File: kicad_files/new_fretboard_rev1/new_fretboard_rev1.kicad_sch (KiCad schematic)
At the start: 22 parts, among them U2 LX3302AQPW-TR-EASY

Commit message: stm32 micro added
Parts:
- added C100: 4.7uf, Capacitor_SMD:C_1206_3216Metric, symbol Device:C_US
- added C101, C102, C103, C104, C105, C106, C108: 100nf, Capacitor_SMD:C_0402_1005Metric, symbol Device:C
- added C107: 1uf, Capacitor_SMD:C_1206_3216Metric, symbol Device:C_US
- added C109, C110: 2.2uf, Capacitor_SMD:C_1206_3216Metric, symbol Device:C_US
- added U10: STM32F730V8Tx, Package_QFP:LQFP-100_14x14mm_P0.5mm, symbol MCU_ST_STM32F7:STM32F730V8Tx
- C12, C13, C14, C15, C16, C17, C18, C19, C20, C21, C22, L5, L6, L7, L8, R10, R12, R13, R8, R9, U2: Component Class ch1 -> (none)
- R11: value 10R -> 10k; Component Class ch1 -> (none)
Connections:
- net GND: now also C100.2, C101.2, C102.2, C103.2, C104.2, C105.2, C106.2, C107.2, C108.2, C109.2, C110.2, U10.10 (VSS), U10.19 (VSSA), U10.26 (VSS), U10.49 (VSS), U10.74 (VSS), U10.99 (VSS)
- net sent9: now reaches C18.2, R12.2
- net sent9: now also U10.77 (PA15)
- new net: C109.1, U10.48 (VCAP_1)
- new net: C110.1, U10.73 (VCAP_2)
- new net +3V3: C100.1, C101.1, C102.1, C103.1, C104.1, C105.1, C106.1, C107.1, C108.1, U10.100 (VDD), U10.11 (VDD), U10.20 (VREF+), U10.21 (VDDA), U10.27 (VDD), U10.50 (VDD), U10.6 (VBAT), U10.75 (VDD)
- new net sent1: U10.39 (PE9)
- new net sent2: U10.41 (PE11)
- new net sent3: U10.43 (PE13)
- new net sent4: U10.44 (PE14)
- new net sent5: U10.59 (PD12)
- new net sent6: U10.60 (PD13)
- new net sent7: U10.64 (PC7)
- new net sent8: U10.66 (PC9)
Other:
- added sheet testchannel8 (testchannel8.kicad_sch)
- sheet testchannel1: file testchannel2.kicad_sch -> testchannel1.kicad_sch
- note added: "needs oscillator for stm32, and programming header, maybe boot pin connections? Also needs 7 more programming headers for the lx3302a ics"

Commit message: mcu configured, still needs power connections and spi i2c connections
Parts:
- added C111: 100nf, Capacitor_SMD:C_0402_1005Metric, symbol Device:C
- added J3: FTSH-107-01-L-DV-K-A, Snapeda:SAMTEC_FTSH-107-01-L-DV-K-A, symbol Snapeda:FTSH-107-01-L-DV-K-A
- added R57, R58: 10k, Resistor_SMD:R_0402_1005Metric, symbol Device:R
- added R59, R60, R62, R65, R68, R69, R70, R71, R72, R78, R80, R82, R84, R86, R88, R90, R92, R94: 1k, Resistor_SMD:R_0402_1005Metric, symbol Device:R
- added R61, R63, R64, R66, R67, R73, R74, R75, R76, R77, R79, R81, R83, R85, R87, R89, R91, R93: 2k, Resistor_SMD:R_0402_1005Metric, symbol Device:R
- added R95: 33R, Resistor_SMD:R_0402_1005Metric, symbol Device:R
- added Y1: ASE-25.000MHZ-LC-T, Snapeda:XTAL_ASE-25.000MHZ-LC-T, symbol Snapeda:ASE-25.000MHZ-LC-T
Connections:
- net +3V3: now also C111.1, J3.03, Y1.4 (VDD)
- net GND: now also C111.2, J3.05, J3.07, R58.2, R61.2, R63.2, R64.2, R66.2, R67.2, R73.1, R74.1, R75.1, R76.1, R77.2, R79.2, R81.2, R83.2, R85.2, R87.2, R89.2, R91.2, R93.2, Y1.2 (GND/CASE)
- net sent1: now also R69.1; no longer U10.39 (PE9)
- net sent2: now also R70.1; no longer U10.41 (PE11)
- net sent3: now also R71.1; no longer U10.43 (PE13)
- net sent4: now also R72.1; no longer U10.44 (PE14)
- net sent5: now also R65.2; no longer U10.59 (PD12)
- net sent6: now also R67.1, R68.1; no longer U10.60 (PD13)
- net sent7: now also R60.1; no longer U10.64 (PC7)
- net sent8: now also R62.1; no longer U10.66 (PC9)
- net sent9: now also R59.1; no longer U10.77 (PA15)
- net at U10.12 (PH0): now also R57.1
- net nrst: now reaches U10.14 (NRST)
- net nrst: now also J3.12
- net SPI1_NSS: now reaches U10.28 (PA4)
- net SPI1_SCK: now reaches U10.29 (PA5)
- net at U10.30 (PA6): now also R95.2
- net SPI1_MOSI: now reaches U10.31 (PA7)
- net PWM5in: now reaches U10.34 (PB0)
- net PWM5in: now also R85.1, R86.2
- net PWM6in: now reaches U10.35 (PB1)
- net PWM6in: now also R87.1, R88.2
- net PWM8in: now reaches U10.46 (PB10)
- net PWM8in: now also R91.1, R92.2
- net PWM9in: now reaches U10.47 (PB11)
- net PWM9in: now also R93.1, R94.2
- net PWM1in: now reaches U10.61 (PD14)
- net PWM1in: now also R77.1, R78.2
- net PWM2in: now reaches U10.62 (PD15)
- net PWM2in: now also R79.1, R80.2
- net PWM3in: now reaches U10.63 (PC6)
- net PWM3in: now also R81.1, R82.2
- net PWM4in: now reaches U10.65 (PC8)
- net PWM4in: now also R83.1, R84.2
- net swdio: now reaches U10.72 (PA13)
- net swdio: now also J3.04
- net swclk: now reaches U10.76 (PA14)
- net swclk: now also J3.06
- net swo: now reaches U10.89 (PB3)
- net swo: now also J3.08
- net PWM7in: now reaches U10.90 (PB4)
- net PWM7in: now also R89.1, R90.2
- net I2C_SCL: now reaches U10.92 (PB6)
- net I2C_SDA: now reaches U10.93 (PB7)
- net at U10.94 (BOOT0): now also R58.1
- net PWM9send: now reaches U2.7 (IO1)
- net PWM9send: now also R94.1
- net GLOBAL_VIN: now reaches C20.2, R13.2
- new net: R62.2, R63.1, U10.66 (PC9)
- new net: R70.2, R74.2, U10.41 (PE11)
- new net: R69.2, R73.2, U10.39 (PE9)
- new net: R57.2, Y1.3 (OUTPUT)
- new net: R59.2, R64.1, U10.77 (PA15)
- new net: R71.2, R75.2, U10.43 (PE13)
- new net: R72.2, R76.2, U10.44 (PE14)
- new net: R65.1, R66.1, U10.59 (PD12)
- new net: R68.2, U10.60 (PD13)
- new net: R60.2, R61.1, U10.64 (PC7)
- new net PWM1send: R78.1
- new net PWM2send: R80.1
- new net PWM3send: R82.1
- new net PWM4send: R84.1
- new net PWM5send: R86.1
- new net PWM6send: R88.1
- new net PWM7send: R90.1
- new net PWM8send: R92.1
- new net SPI1_MISO: R95.1
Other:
- note removed: "needs oscillator for stm32, and programming header, maybe boot pin connections? Also needs 7 more programming headers for the lx3302a ics"

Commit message: finished routing - adding silkscreen
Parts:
- added C112, C113: 1uf, Capacitor_SMD:C_1206_3216Metric, symbol Device:C_US
- added J10: 530470410, Snapeda:CONN04_530470410_MOL, symbol Snapeda:530470410
- added J11, J12, J13: 110990030, Snapeda:SEEED_110990030, symbol Snapeda:110990030
- added R103: 10k, Resistor_SMD:R_0402_1005Metric, symbol Device:R
- added R96: 0R, Resistor_SMD:R_1206_3216Metric, symbol Device:R
- added TP1, TP2, TP3, TP4: TestPoint, Connector_PinHeader_1.00mm:PinHeader_1x01_P1.00mm_Vertical, symbol Connector:TestPoint
- added U11: MIC5504-3.3YM5, Package_TO_SOT_SMD:SOT-23-5, symbol Regulator_Linear:MIC5504-3.3YM5
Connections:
- net +3V3: now also C112.1, U11.5 (VOUT)
- net GLOBAL_VIN: now also J13.1, J13.2, R96.2
- net GND: now also C112.2, C113.2, J10.1, J11.4, J13.3, J13.4, U11.2 (GND)
- net I2C_SCL: now also J11.1
- net I2C_SDA: now also J11.2
- net PWM1in: now also U10.34 (PB0); no longer U10.61 (PD14)
- net PWM2in: now also U10.35 (PB1); no longer U10.62 (PD15)
- net PWM3in: now also U10.46 (PB10); no longer U10.63 (PC6)
- net PWM4in: now also U10.47 (PB11); no longer U10.65 (PC8)
- net PWM5in: now also U10.61 (PD14); no longer U10.34 (PB0)
- net PWM6in: now also U10.62 (PD15); no longer U10.35 (PB1)
- net PWM7in: now also TP2.1; no longer U10.90 (PB4)
- net PWM8in: now also TP1.1; no longer U10.46 (PB10)
- net PWM9in: now also U10.90 (PB4); no longer U10.47 (PB11)
- net SPI1_MISO: now also J12.3
- net SPI1_MOSI: now also J12.4
- net SPI1_NSS: now also J12.2
- net SPI1_SCK: now also J12.1
- net VIN_A: now also J10.2, R103.2
- net IO3: now reaches U2.3 (IO3)
- net IO3: now also J10.3, R103.1
- net IO2: now reaches C19.2, R11.1, R12.1, U2.6 (IO2)
- net IO2: now also J10.4
- new net: TP3.1, U10.63 (PC6)
- new net: TP4.1, U10.65 (PC8)
- new net GLOBAL_VIN2: C113.1, R96.1, U11.1 (VIN), U11.3 (EN)

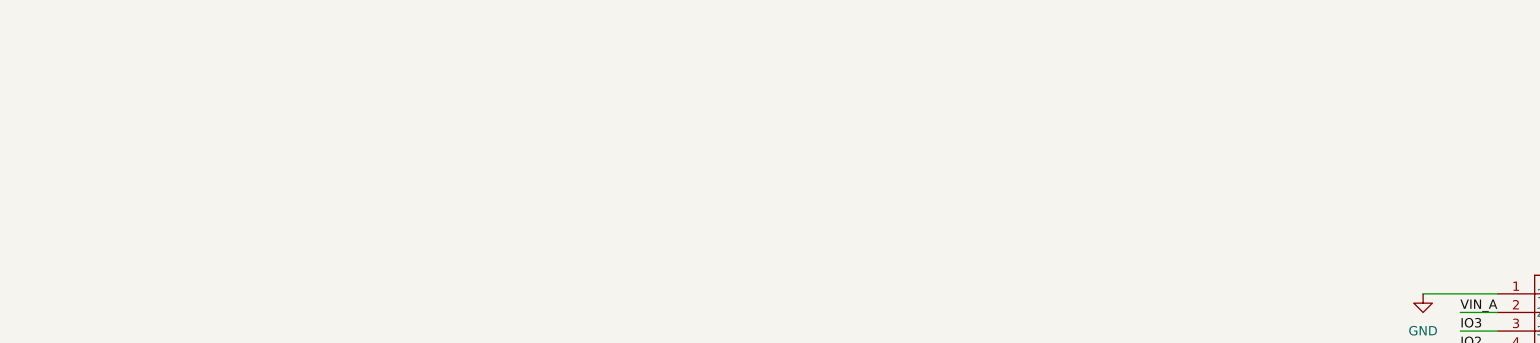
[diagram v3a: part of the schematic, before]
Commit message: mostly done, adjusting silkscreen labels
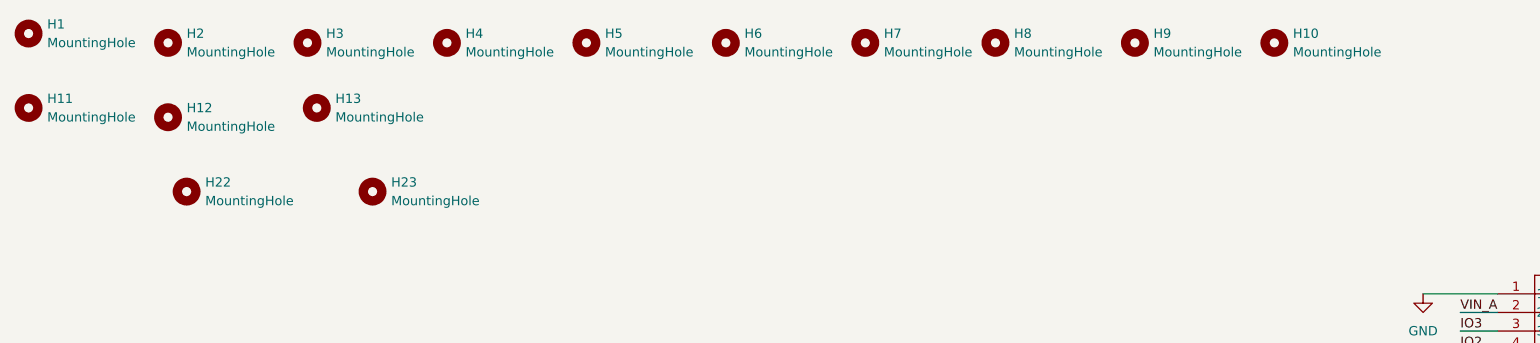
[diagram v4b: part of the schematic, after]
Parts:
- added H1, H10, H11, H12, H13, H2, H22, H23, H3, H4, H5, H6, H7, H8, H9: MountingHole, MountingHole:MountingHole_2.1mm, symbol Mechanical:MountingHole

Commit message: exported gerbers of lefthand
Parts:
- added J14: Conn_01x05, Connector_PinSocket_2.54mm:PinSocket_1x05_P2.54mm_Vertical, symbol Connector_Generic:Conn_01x05
- added J15, J16, J17: Conn_01x02_Pin, Connector_PinSocket_2.54mm:PinSocket_1x02_P2.54mm_Vertical, symbol Connector:Conn_01x02_Pin
- added R104, R105: 2k, Resistor_SMD:R_0402_1005Metric, symbol Device:R
- L5, L6, L7, L8: now left out of the parts list
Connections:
- net +3V3: now also J16.1 (Pin_1)
- net GND: now also J16.2 (Pin_2), J17.2 (Pin_2)
- net I2C_SCL: now also R104.1
- net I2C_SDA: now also R105.1
- net at J11.3: now also J17.1 (Pin_1), R104.2, R105.2
- net at U10.1 (PE2): now also J14.5 (Pin_5)
- net at U10.2 (PE3): now also J14.4 (Pin_4)
- net at U10.3 (PE4): now also J14.3 (Pin_3)
- net at U10.4 (PE5): now also J14.2 (Pin_2)
- net at U10.5 (PE6): now also J14.1 (Pin_1)
- net at U10.97 (PE0): now also J15.1 (Pin_1)
- net at U10.98 (PE1): now also J15.2 (Pin_2)
